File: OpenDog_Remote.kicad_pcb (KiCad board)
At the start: 2 copper layers, 81 x 51 mm, 56 parts, among them J1 Conn_01x03_Pin, J10 Conn_01x03_Pin, J11 Conn_01x03_Pin, J12 Conn_01x02_Pin, J13 Conn_01x03_Pin, J14 Conn_01x03_Pin, J15 Conn_01x03_Pin, J16 Conn_01x03_Pin, J17 NRF, J18 Conn_02x08_Odd_Even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

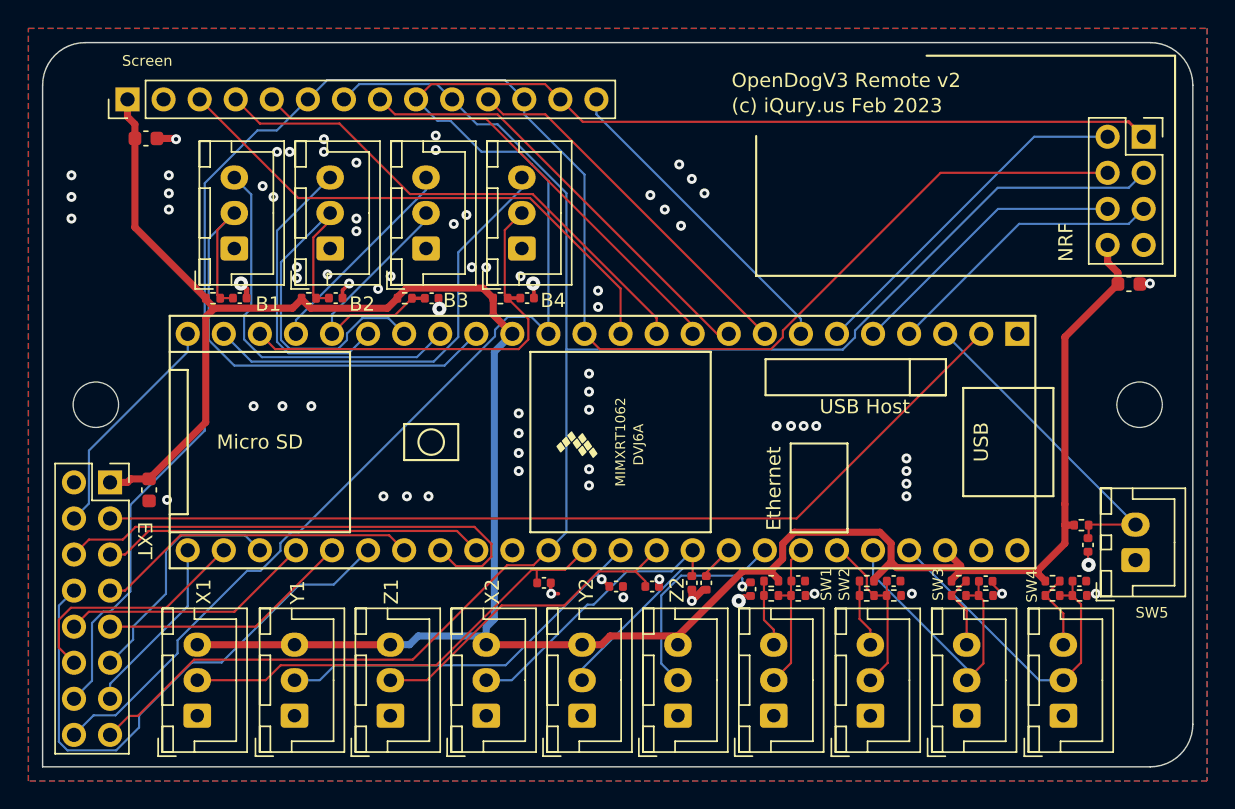
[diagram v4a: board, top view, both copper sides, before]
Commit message: Separate screen and NRF/Touch SPI channels.
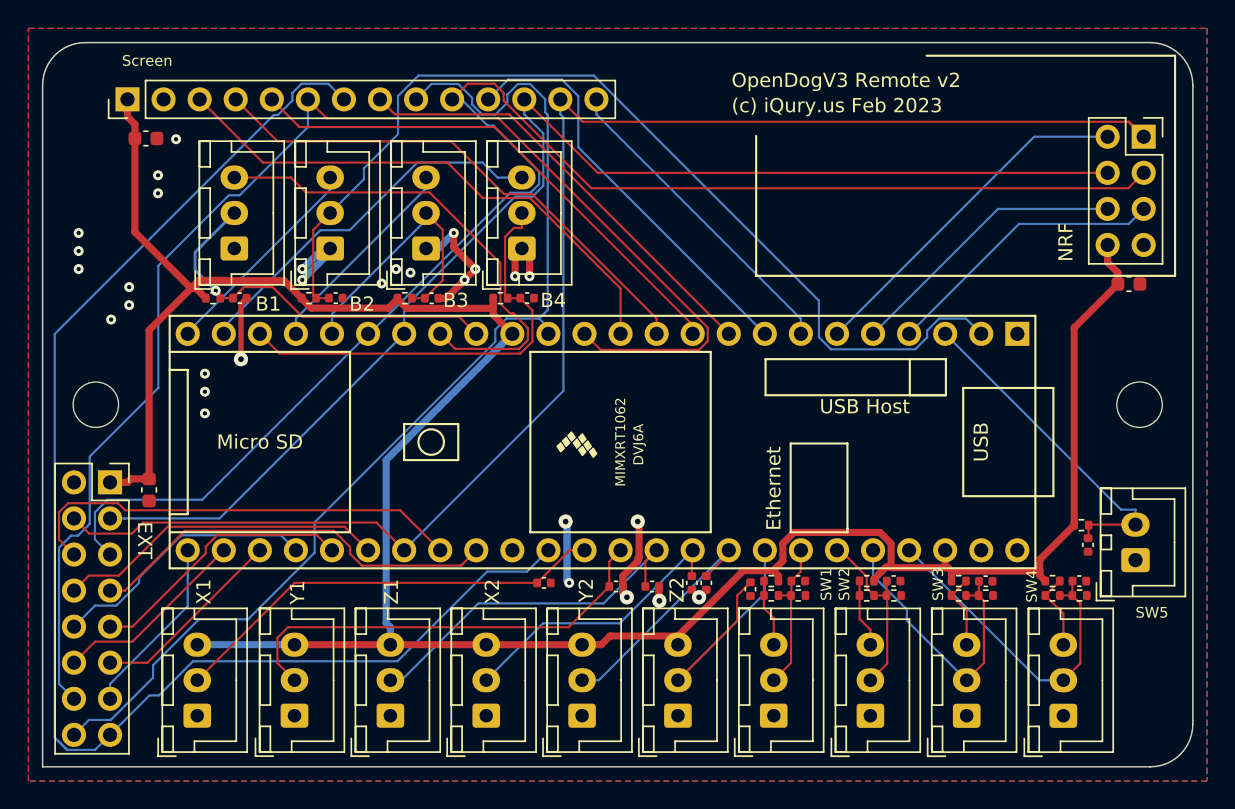
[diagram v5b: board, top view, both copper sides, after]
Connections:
- J17 pad 1: /MISO -> /MISO2
- J17 pad 3: /SCK -> /SCK2
- J17 pad 4: /MOSI -> /MOSI2
- J18 pad 3: /EX1 -> /MOSI2
- J18 pad 4: /EX2 -> /MISO2
- J18 pad 5: /EX3 -> /SCK2
- J18 pad 7: /EX5 -> /EX3
- J7 pad 10: /SCK -> /SCK2
- J7 pad 12: /MOSI -> /MOSI2
- J7 pad 13: /MISO -> /MISO2
- U1 pad 18: /B2 -> /MOSI2
- U1 pad 19: /B2_LED -> /SCK2
- U1 pad 2: /EX1 -> /B2
- U1 pad 24: /EX2 -> /B2_LED
- U1 pad 31: /EX5 -> /MISO2
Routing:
- net /SCK2: track 0.00 -> 106.4 mm
- net /MISO2: track 0.00 -> 103.5 mm
- net /MOSI2: track 0.00 -> 91.2 mm
- net /EX1: track 66.7 -> 0.00 mm
- net /MISO: track 122.9 -> 76.7 mm
- net /B2: track 28.4 -> 70.5 mm
- net /MOSI: track 127.5 -> 95.8 mm
- net /SCK: track 127.3 -> 98.7 mm
- net GND: track 12.1 -> 35.6 mm, vias 75 -> 29
- net /EX5: track 22.8 -> 0.00 mm
- net /EX2: track 16.3 -> 0.00 mm
- net /EX6: track 39.4 -> 23.3 mm
- net /B1: track 37.7 -> 27.6 mm, vias 0 -> 1
- net /B1_LED: track 27.1 -> 34.4 mm
- net /B2_LED: track 20.4 -> 15.2 mm
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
